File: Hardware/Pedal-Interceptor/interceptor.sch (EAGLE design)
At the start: 44 parts, among them U1 STM32-M-64-LQFP, U2 MIC5233-5.0YM5-TR, U3 MIC5233-3.3YM5-TR, U4 TJA1042HVSON, U6 MCP6002, Y1 16MHz

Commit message: Pedal fix
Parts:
- added SJ1: (no value), jumper:SJ2W
- added U5: MIC5233-5.0YM5-TR, SamacSys_Parts:MIC5233-5.0YM5-TR
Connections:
- new net N$12: SJ1.2, U$3.6
- new net N$14: SJ1.1, U5.OUT
- net 5V: now also SJ1.3, U5.EN, U5.IN; no longer U$3.6
- net GND: now also U5.GND
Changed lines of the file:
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@@
 <setting verticaltext="up"/>
 </settings>
-<grid distance="0.1" unitdist="inch" unit="inch" style="dots" multiple="1" display="yes" altdistance="5" altunitdist="mil" altunit="mil"/>
+<grid distance="0.1" unitdist="inch" unit="inch" style="lines" multiple="1" display="no" altdistance="0.01" altunitdist="inch" altunit="inch"/>
 <layers>
 <layer number="1" name="Top" color="4" fill="1" visible="no" active="no"/>
@@
 <part name="U$3" library="interceptor" deviceset="MICROFIT-6" device=""/>
 <part name="SUPPLY8" library="SparkFun-Aesthetics" library_urn="urn:adsk.eagle:library:507" deviceset="VCC" device="" value="3V3"/>
+<part name="U5" library="SamacSys_Parts" deviceset="MIC5233-5.0YM5-TR" device=""/>
+<part name="SJ1" library="jumper" library_urn="urn:adsk.eagle:library:252" deviceset="SJ2W" device="" package3d_urn="urn:adsk.eagle:package:15474/1"/>
 </parts>
 <sheets>
@@
 <attribute name="VALUE" x="147.574" y="85.09" size="1.778" layer="96"/>
 </instance>
+<instance part="U5" gate="G$1" x="238.76" y="58.42" smashed="yes">
+<attribute name="NAME" x="260.35" y="66.04" size="1.778" layer="95" align="center-left"/>
+<attribute name="VALUE" x="260.35" y="63.5" size="1.778" layer="96" align="center-left"/>
+</instance>
+<instance part="SJ1" gate="G$1" x="248.92" y="68.58" smashed="yes" rot="R270">
+<attribute name="NAME" x="249.301" y="66.04" size="1.778" layer="95" rot="R270"/>
+<attribute name="VALUE" x="247.015" y="66.04" size="1.778" layer="96" rot="R270"/>
+</instance>
 </instances>
 <busses>
@@
 <pinref part="C5" gate="G$1" pin="2"/>
 <wire x1="184.15" y1="51.054" x2="219.71" y2="51.054" width="0.1524" layer="91"/>
+<pinref part="U5" gate="G$1" pin="GND"/>
+<wire x1="238.76" y1="55.88" x2="228.6" y2="55.88" width="0.1524" layer="91"/>
+<wire x1="228.6" y1="55.88" x2="228.6" y2="50.8" width="0.1524" layer="91"/>
+<wire x1="228.6" y1="50.8" x2="224.79" y2="50.8" width="0.1524" layer="91"/>
+<wire x1="224.79" y1="50.8" x2="224.79" y2="51.054" width="0.1524" layer="91"/>
+<junction x="224.79" y="51.054"/>
 </segment>
 <segment>
@@
 </segment>
 <segment>
-<wire x1="259.08" y1="76.2" x2="243.84" y2="76.2" width="0.1524" layer="91"/>
-<label x="243.84" y="76.2" size="1.778" layer="95"/>
-<pinref part="U$3" gate="G$1" pin="6"/>
-</segment>
-<segment>
 <wire x1="40.64" y1="121.92" x2="40.64" y2="124.46" width="0.1524" layer="91"/>
 <wire x1="35.56" y1="121.92" x2="40.64" y2="121.92" width="0.1524" layer="91"/>
 <pinref part="D1" gate="1" pin="C"/>
 <label x="40.64" y="124.46" size="1.778" layer="95"/>
+</segment>
+<segment>
+<pinref part="SJ1" gate="G$1" pin="3"/>
+<wire x1="243.84" y1="68.58" x2="241.3" y2="68.58" width="0.1524" layer="91"/>
+<label x="241.3" y="68.58" size="1.778" layer="95" rot="R180"/>
+</segment>
+<segment>
+<pinref part="U5" gate="G$1" pin="EN"/>
+<wire x1="238.76" y1="53.34" x2="233.68" y2="53.34" width="0.1524" layer="91"/>
+<wire x1="233.68" y1="53.34" x2="233.68" y2="58.42" width="0.1524" layer="91"/>
+<pinref part="U5" gate="G$1" pin="IN"/>
+<wire x1="233.68" y1="58.42" x2="238.76" y2="58.42" width="0.1524" layer="91"/>
+<label x="233.68" y="58.42" size="1.778" layer="95"/>
 </segment>
 </net>
@@
 </segment>
 </net>
+<net name="N$12" class="0">
+<segment>
+<pinref part="SJ1" gate="G$1" pin="2"/>
+<pinref part="U$3" gate="G$1" pin="6"/>
+<wire x1="248.92" y1="73.66" x2="248.92" y2="76.2" width="0.1524" layer="91"/>
+<wire x1="248.92" y1="76.2" x2="259.08" y2="76.2" width="0.1524" layer="91"/>
+</segment>
+</net>
+<net name="N$14" class="0">
+<segment>
+<pinref part="SJ1" gate="G$1" pin="1"/>
+<wire x1="254" y1="68.58" x2="269.24" y2="68.58" width="0.1524" layer="91"/>
+<wire x1="269.24" y1="68.58" x2="269.24" y2="55.88" width="0.1524" layer="91"/>
+<pinref part="U5" gate="G$1" pin="OUT"/>
+<wire x1="269.24" y1="55.88" x2="264.16" y2="55.88" width="0.1524" layer="91"/>
+</segment>
+</net>

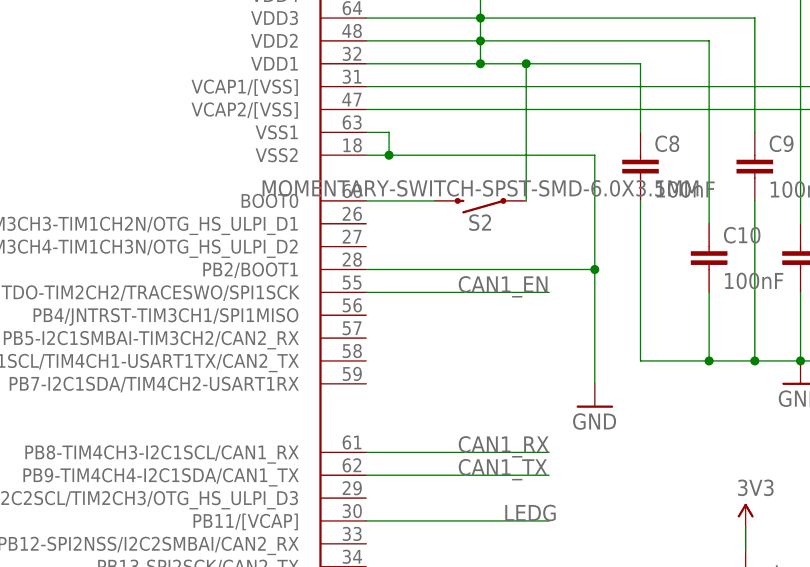
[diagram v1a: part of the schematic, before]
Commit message: add pull resistors
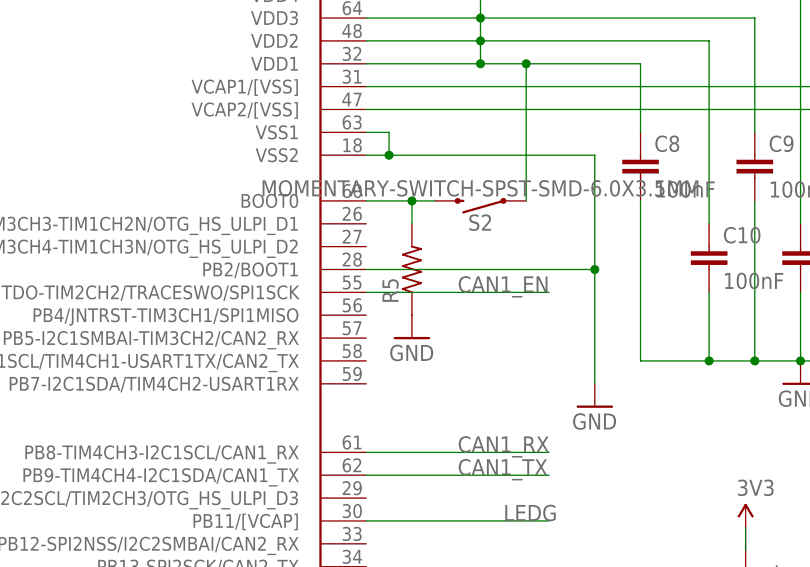
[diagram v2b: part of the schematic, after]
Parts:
- added R5: (no value), comma.ai:R0402
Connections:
- net GND: now also R5.1
- net N$7: now also R5.2
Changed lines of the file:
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@@
 <part name="U5" library="SamacSys_Parts" deviceset="MIC5233-5.0YM5-TR" device=""/>
 <part name="SJ1" library="jumper" library_urn="urn:adsk.eagle:library:252" deviceset="SJ2W" device="" package3d_urn="urn:adsk.eagle:package:15474/1"/>
+<part name="R5" library="comma.ai" deviceset="R" device="0402"/>
+<part name="GND7" library="SparkFun-Aesthetics" library_urn="urn:adsk.eagle:library:507" deviceset="GND" device=""/>
 </parts>
 <sheets>
@@
 <attribute name="VALUE" x="247.015" y="66.04" size="1.778" layer="96" rot="R270"/>
 </instance>
+<instance part="R5" gate="G$1" x="190.5" y="149.86" smashed="yes" rot="R90">
+<attribute name="NAME" x="189.0014" y="146.05" size="1.778" layer="95" rot="R90"/>
+<attribute name="VALUE" x="193.802" y="146.05" size="1.778" layer="96" rot="R90"/>
+</instance>
+<instance part="GND7" gate="1" x="190.5" y="142.24" smashed="yes">
+<attribute name="VALUE" x="187.96" y="139.7" size="1.778" layer="96"/>
+</instance>
 </instances>
 <busses>
@@
 <label x="243.84" y="81.28" size="1.778" layer="95"/>
 <pinref part="U$3" gate="G$1" pin="4"/>
+</segment>
+<segment>
+<pinref part="R5" gate="G$1" pin="1"/>
+<pinref part="GND7" gate="1" pin="GND"/>
 </segment>
 </net>
@@
 <pinref part="S2" gate="G$1" pin="2"/>
 <pinref part="U1" gate="G$1" pin="BOOT0"/>
-<wire x1="193.04" y1="157.48" x2="185.42" y2="157.48" width="0.1524" layer="91"/>
-</segment>
-</net>
+<wire x1="193.04" y1="157.48" x2="190.5" y2="157.48" width="0.1524" layer="91"/>
+<pinref part="R5" gate="G$1" pin="2"/>
+<wire x1="190.5" y1="157.48" x2="185.42" y2="157.48" width="0.1524" layer="91"/>
+<wire x1="190.5" y1="154.94" x2="190.5" y2="157.48" width="0.1524" layer="91"/>
+<junction x="190.5" y="157.48"/>
+</segment>
+</net>
